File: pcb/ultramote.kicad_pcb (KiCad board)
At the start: 2 copper layers, 40 x 42.5 mm, 59 parts, among them J1 U.FL-R-SMT-1, J2 SM02B-SRSS-TB, J3 USB-C-XKB_U262-16XN, J5 WST-REDFIT-4P, J6 PJ-242D-SMT, J7 PJ-242D-SMT, Q1 2N7002, Q2 BSS84, SW1 SSSS211603, U1 LoRa-E5, U2 TPS2112APW, U3 MCP73831-5-OT, U4 TLV70233DBVT, U5 CH340N, U6 EL357, U7 EL357

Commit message: Add logo to PCB backside
- closes #3
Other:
- board text added: "Ultramote Rev ${REVISION} 02|2023"

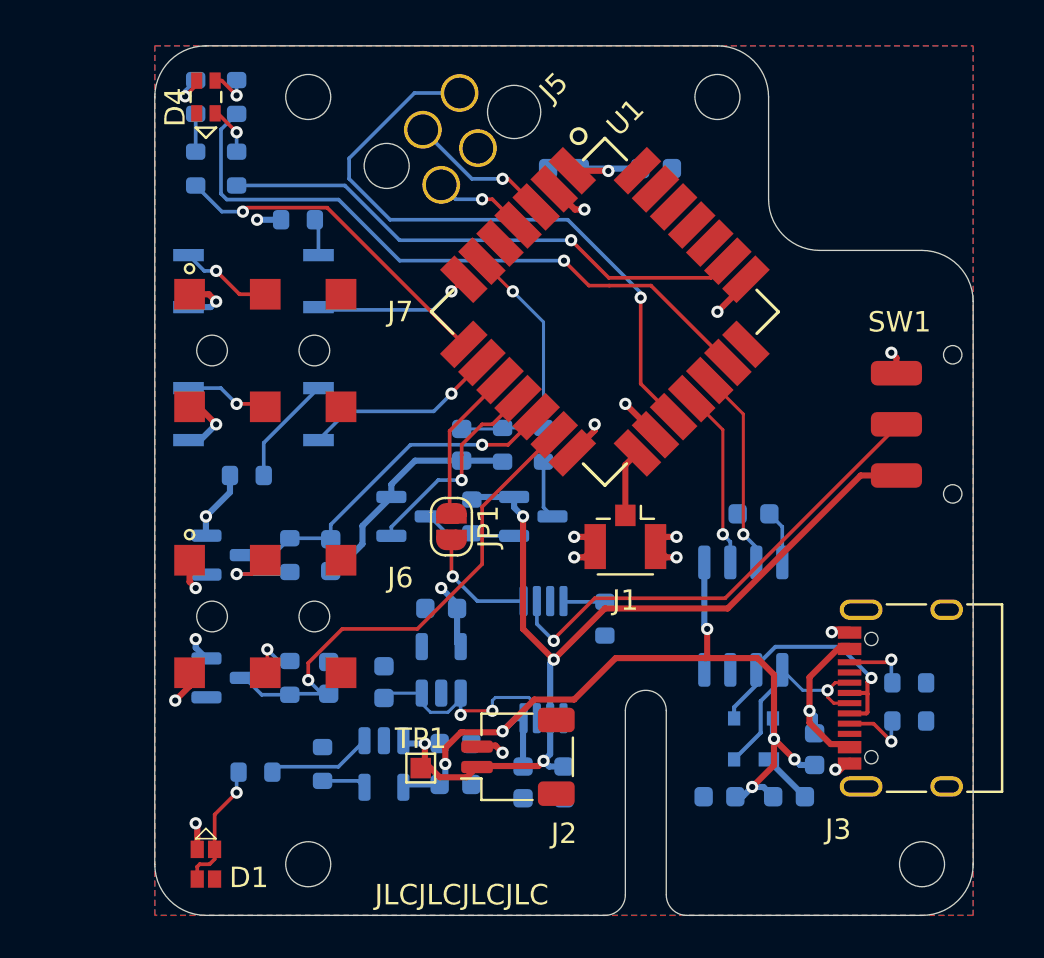
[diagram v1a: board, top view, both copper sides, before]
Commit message: Migrate project to KiCad v7
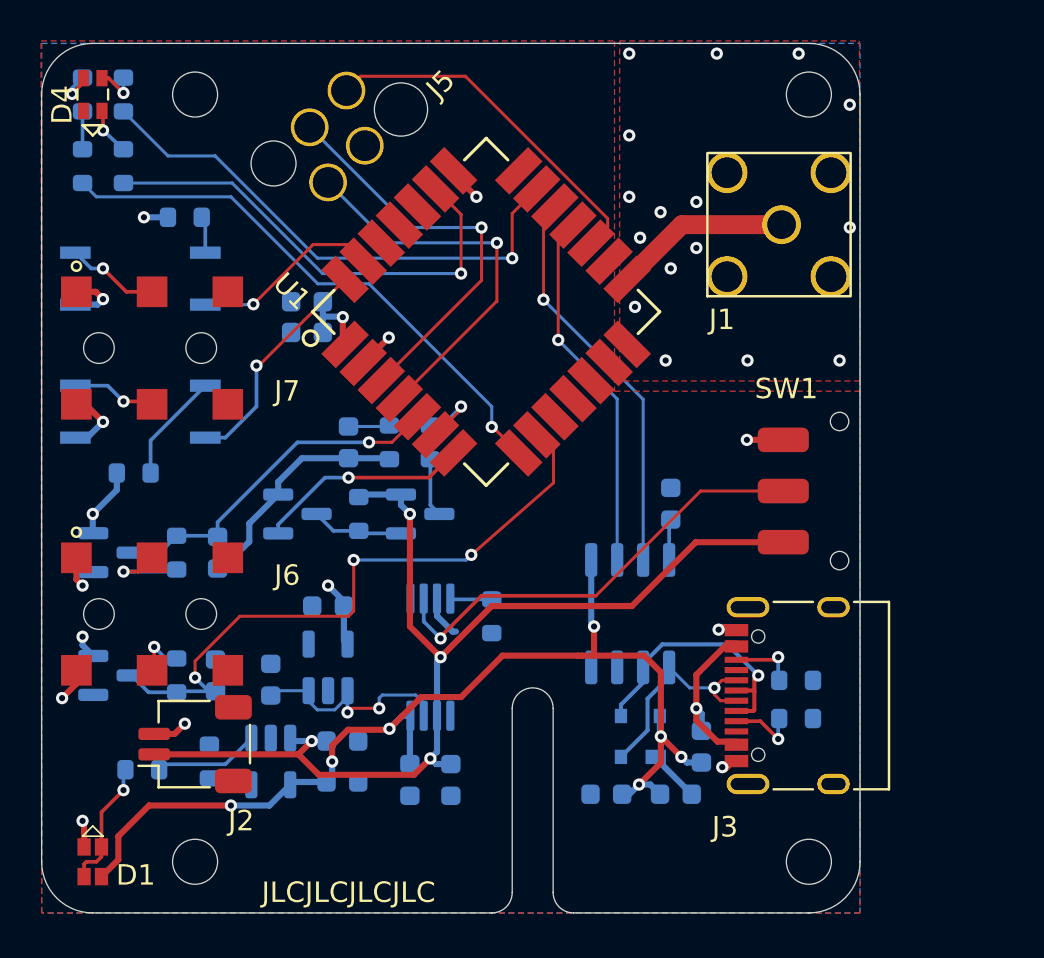
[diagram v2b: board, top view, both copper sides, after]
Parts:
- removed JP1: SolderJumper_2_Open, Jumper:SolderJumper-2_P1.3mm_Open_RoundedPad1.0x1.5mm
- removed TP1: TestPoint, TestPoint:TestPoint_Pad_1.0x1.0mm
- J1: value U.FL-R-SMT-1 -> SMA-KWE902; footprint Connector_Coaxial:U.FL_Hirose_U.FL-R-SMT-1_Vertical -> ultramote:SMA-KWE902
- moved C1 18.8 mm to (100.5, 71.1), turned to 180 degrees
- moved J1 17.0 mm to (123.5, 65.9), turned to 90 degrees
- moved J2 15.8 mm to (95.0, 91.2)
- moved C2 14.1 mm to (100.5, 69.6)
- moved SW1 6.42 mm to (126.5, 78.9)
- moved U1 5.80 mm to (109.2, 70.1), turned to 45 degrees
- moved C10 5.53 mm to (115.1, 93.7)
- moved C11 5.53 mm to (118.5, 93.7)
- moved C13 5.53 mm to (96.1, 81.9)
- moved C14 5.53 mm to (96.0, 87.9)
- moved C3 5.53 mm to (102.5, 76.5)
- moved C4 5.53 mm to (107.5, 93.0)
- moved C5 5.53 mm to (105.5, 93.0)
- moved C6 5.53 mm to (98.7, 88.1)
- moved C7 5.53 mm to (101.5, 84.5)
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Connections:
- D1 pad 2: +3V3 -> VBUS
- Q1 pad 1: /BATTERY_VDIV -> /BATTERY_DIVIDER_ON
- U1 pad 10: /PWR_MUX_STATUS -> unconnected-(U1-PB6-Pad10)
- U1 pad 11: /BATTERY_VDIV -> unconnected-(U1-PB5-Pad11)
- U1 pad 12: /INPUT_SLEEVE -> unconnected-(U1-PC1-Pad12)
- U1 pad 13: /INPUT_TIP -> unconnected-(U1-PC0-Pad13)
- U1 pad 27: unconnected-(U1-Pad27) -> /OUTPUT_SLEEVE
- U1 pad 28: unconnected-(U1-Pad28) -> /OUTPUT_TIP
- U1 pad 5: unconnected-(U1-Pad5) -> /INPUT_SLEEVE
- U1 pad 7: /OUTPUT_SLEEVE -> /BATTERY_DIVIDER_ON
- U1 pad 9: /OUTPUT_TIP -> /INPUT_TIP
- U2 pad 1: Net-(JP1-Pad2) -> unconnected-(U2-STAT-Pad1)
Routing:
- net /SWDCLK: track 4.57 -> 19.1 mm
- net /nRST: track 31.0 -> 17.5 mm, vias 1 -> 0
- net /SWDIO: track 7.10 -> 19.9 mm
- net VBUS: track 41.7 -> 53.5 mm, vias 6 -> 7
- net /LED_R: track 16.5 -> 27.4 mm
- net /BATTERY_DIVIDER_ON: track 0.00 -> 10.5 mm, vias 0 -> 1
- net /BATTERY_VDIV: track 10.2 -> 0.00 mm, vias 1 -> 0
- net /USB/MCU_UART_TX: track 9.83 -> 19.5 mm
- net /USB/MCU_UART_RX: track 8.79 -> 17.9 mm
- net /PWR_MUX_STATUS: track 7.55 -> 0.00 mm
- net /INPUT_TIP: track 24.9 -> 31.7 mm, vias 1 -> 3
- net /LED_G: track 32.4 -> 25.9 mm
- net +BATT: track 46.8 -> 53.2 mm
- net GND: track 41.9 -> 35.5 mm, vias 17 -> 27
- net Net-(JP1-Pad2): track 5.77 -> 0.00 mm, vias 1 -> 0
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- added copper zone on F.Cu, net GND
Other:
- outline, holes or cut-outs redrawn
- board text removed: "Ultramote Rev ${REVISION} 02|2023"
